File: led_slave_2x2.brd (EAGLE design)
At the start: 45.7 x 40.3 mm, 30 parts, among them U1 WS2801, U2 WS2801, U3 WS2801, U4 WS2801

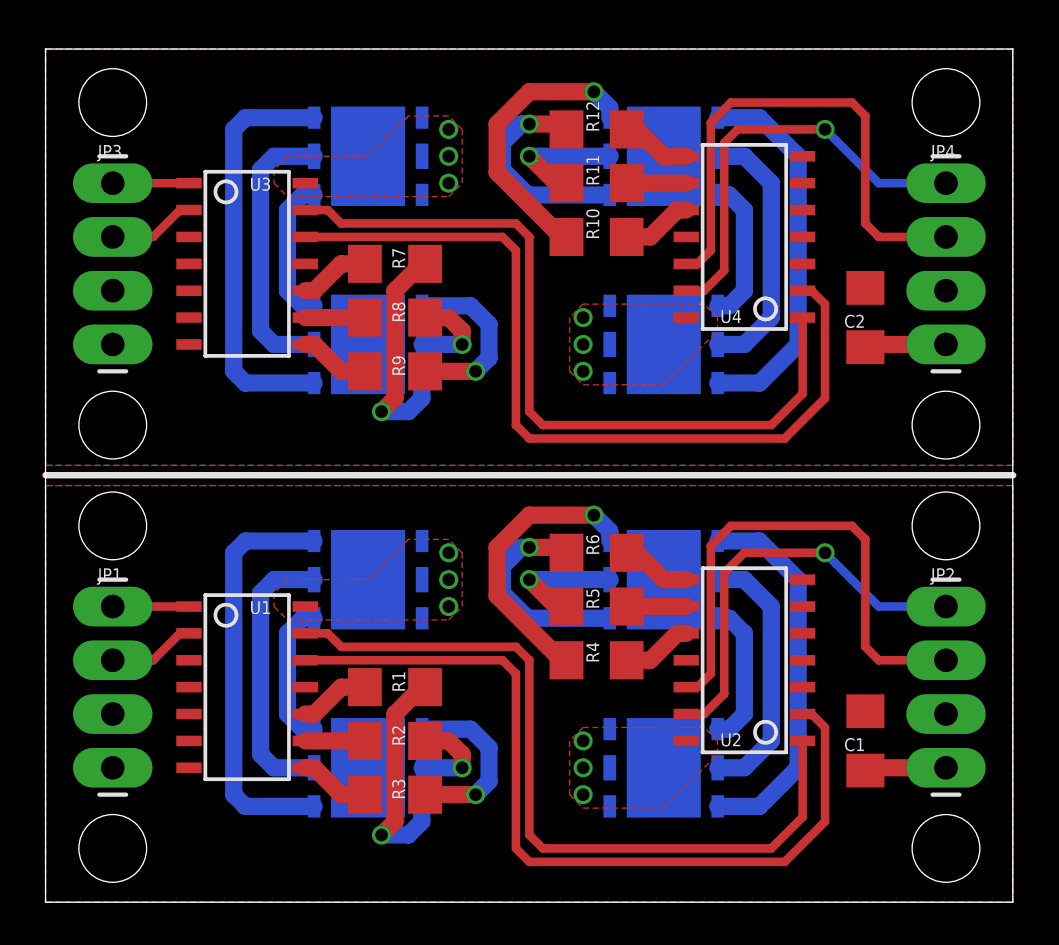
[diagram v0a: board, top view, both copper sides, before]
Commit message: fixed spacing and ground plain power concerns
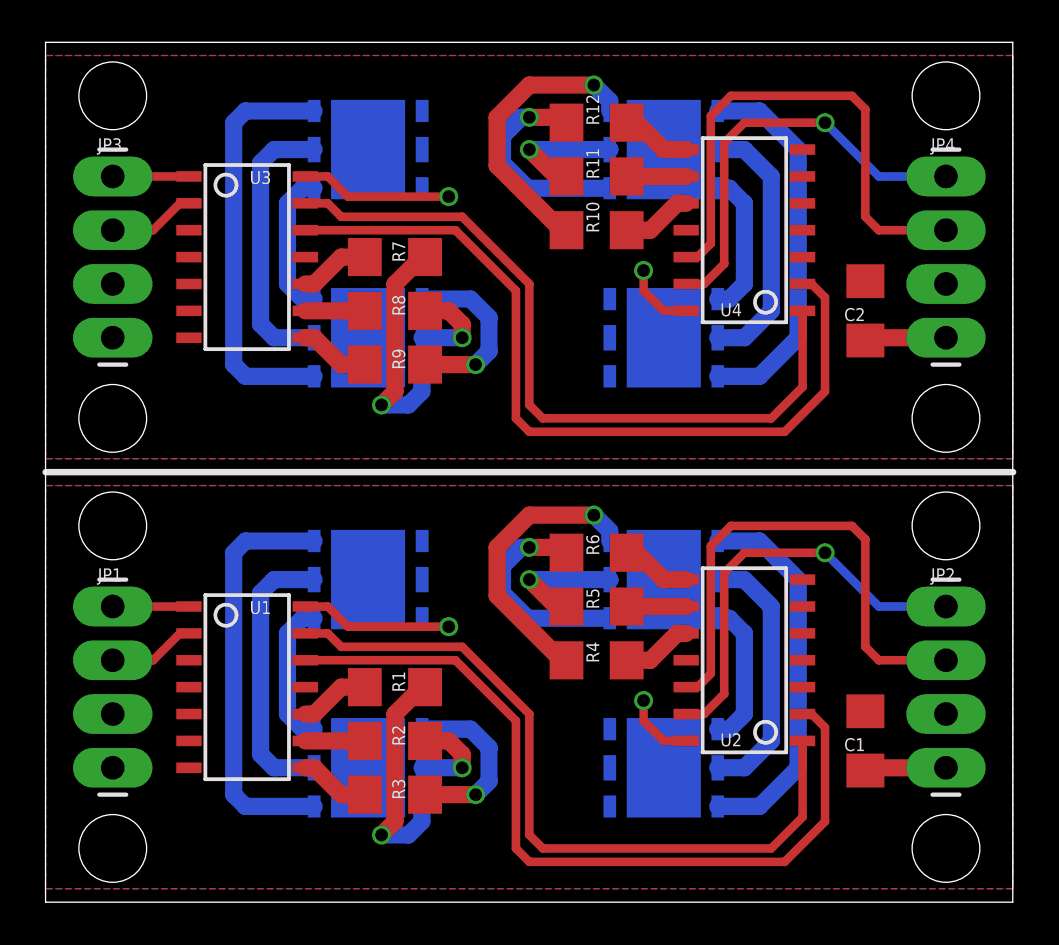
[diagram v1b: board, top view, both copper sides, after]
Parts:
- moved C2 0.32 mm to (38.7, 27.9)
- moved JP3 0.32 mm to (3.17, 26.7)
- moved JP4 0.32 mm to (42.5, 26.7)
- moved LED5 0.32 mm to (15.2, 26.7)
- moved LED6 0.32 mm to (15.2, 35.6)
- moved LED7 0.32 mm to (29.2, 35.6)
- moved LED8 0.32 mm to (29.2, 26.7)
- moved R11 0.32 mm to (26.0, 34.3)
- moved R8 0.32 mm to (16.5, 27.9)
- moved R10 0.32 mm to (26.0, 31.8)
- moved R7 0.32 mm to (16.5, 30.5)
- moved R9 0.32 mm to (16.5, 25.4)
- moved U3 0.32 mm to (9.53, 30.5)
- moved U4 0.32 mm to (33.0, 31.8)
- moved R12 0.32 mm to (26.0, 36.8)
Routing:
- net N$53: track 3.86 -> 14.4 mm, vias 6 -> 2
- net N$26: track 3.86 -> 14.4 mm, vias 6 -> 2
- net N$28: track 36.8 -> 35.3 mm
- net N$3: track 36.8 -> 35.3 mm
- net N$4: track 39.9 -> 38.6 mm
- net N$29: track 39.9 -> 38.6 mm
- removed copper zone on layer 1, net N$26
- removed copper zone on layer 1, net N$53
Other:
- board size 45.7 x 40.3 mm -> 45.7 x 40.6 mm
